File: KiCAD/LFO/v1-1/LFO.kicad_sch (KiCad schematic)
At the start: 20 parts, among them J1 OUT, J2 OUT, J3 Conn_01x03, J4 Conn_01x03, SW1 SW_SPDT, SW2 SW_SPDT, U1 TL072, U2 TL072

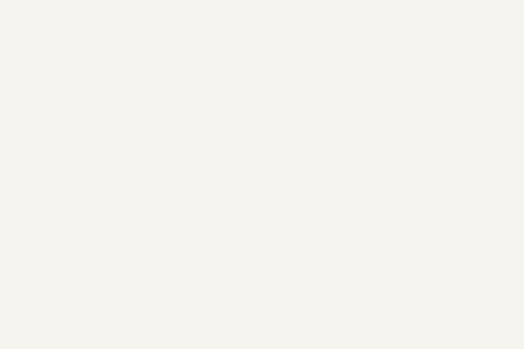
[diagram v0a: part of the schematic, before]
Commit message: Footprint Edits
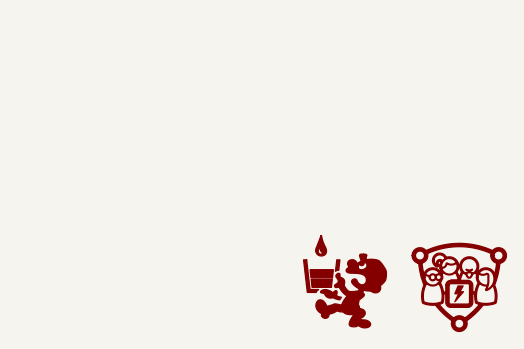
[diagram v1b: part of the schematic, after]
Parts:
- added G1: ~, symbol HackSynth:CCHS_Logo
- added G2: ~, symbol HackSynth:Logo_PancakeLegend
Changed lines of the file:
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@@
+	)
+	(symbol
+		(lib_id "HackSynth:CCHS_Logo")
+		(at 275.59 172.72 0)
+		(unit 1)
+		(exclude_from_sim no)
+		(in_bom yes)
+		(on_board yes)
+		(dnp no)
+		(fields_autoplaced yes)
+		(property "Reference" "G1"
+			(at 275.59 180.34 0)
+			(effects
+				(font
+					(size 1.27 1.27)
+				)
+				(hide yes)
+			)
+		)
+		(property "Value" "~"
+			(at 281.94 173.89 0)
+			(effects
+				(font
+					(size 1.27 1.27)
+				)
+				(justify left)
+			)
+		)
+		(property "Footprint" ""
+			(at 275.59 172.72 0)
+			(effects
+				(font
+					(size 1.27 1.27)
+				)
+				(hide yes)
+			)
+		)
+		(property "Datasheet" ""
+			(at 275.59 172.72 0)
+			(effects
+				(font
+					(size 1.27 1.27)
+				)
+				(hide yes)
+			)
+		)
+		(property "Description" ""
+			(at 275.59 172.72 0)
+			(effects
+				(font
+					(size 1.27 1.27)
+				)
+				(hide yes)
+			)
+		)
+		(instances
+			(project "LFO"
+				(path "/cf31493f-2592-4a10-a419-2df89491bd24"
+					(reference "G1")
+					(unit 1)
+				)
+			)
+		)
 	)
 	(symbol
@@
 				)
 			)
+		)
+	)
+	(symbol
+		(lib_id "HackSynth:Logo_PancakeLegend")
+		(at 262.89 173.355 0)
+		(unit 1)
+		(exclude_from_sim no)
+		(in_bom yes)
+		(on_board yes)
+		(dnp no)
+		(fields_autoplaced yes)
+		(property "Reference" "G2"
+			(at 262.89 180.975 0)
+			(effects
+				(font
+					(size 1.27 1.27)
+				)
+				(hide yes)
+			)
+		)
+		(property "Value" "~"
+			(at 269.24 173.2549 0)
+			(effects
+				(font
+					(size 1.27 1.27)
+				)
+				(justify left)
+			)
+		)
+		(property "Footprint" ""
+			(at 262.89 173.355 0)
+			(effects
+				(font
+					(size 1.27 1.27)
+				)
+				(hide yes)
+			)
+		)
+		(property "Datasheet" ""
+			(at 262.89 173.355 0)
+			(effects
+				(font
+					(size 1.27 1.27)
+				)
+				(hide yes)
+			)
+		)
+		(property "Description" ""
+			(at 262.89 173.355 0)
+			(effects
+				(font
+					(size 1.27 1.27)
+				)
+				(hide yes)
+			)
+		)
+		(instances
+			(project "LFO"
+				(path "/cf31493f-2592-4a10-a419-2df89491bd24"
+					(reference "G2")
+					(unit 1)
+				)
+			)
